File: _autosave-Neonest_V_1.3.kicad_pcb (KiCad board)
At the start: 2 copper layers, 75 x 88 mm, 99 parts, among them J3 693071010811, J5 Conn_01x02, J6 Conn_01x05, J7 Conn_01x03, Q1 BC817, Q2 BC817, Q3 STB33N65M2, Q4 BC817, Q5 STB33N65M2, Q6 STB33N65M2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

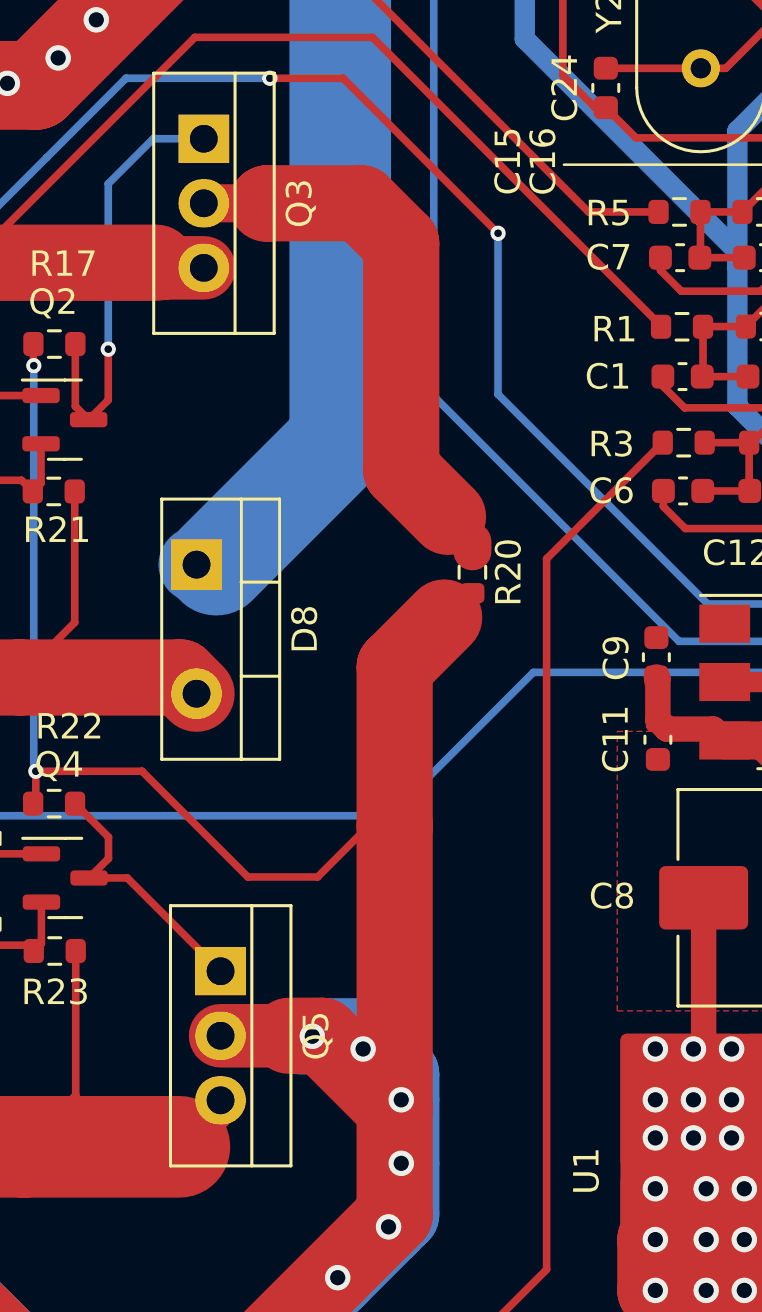
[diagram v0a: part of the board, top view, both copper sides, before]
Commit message: Formatted schematic and Increased power tracks
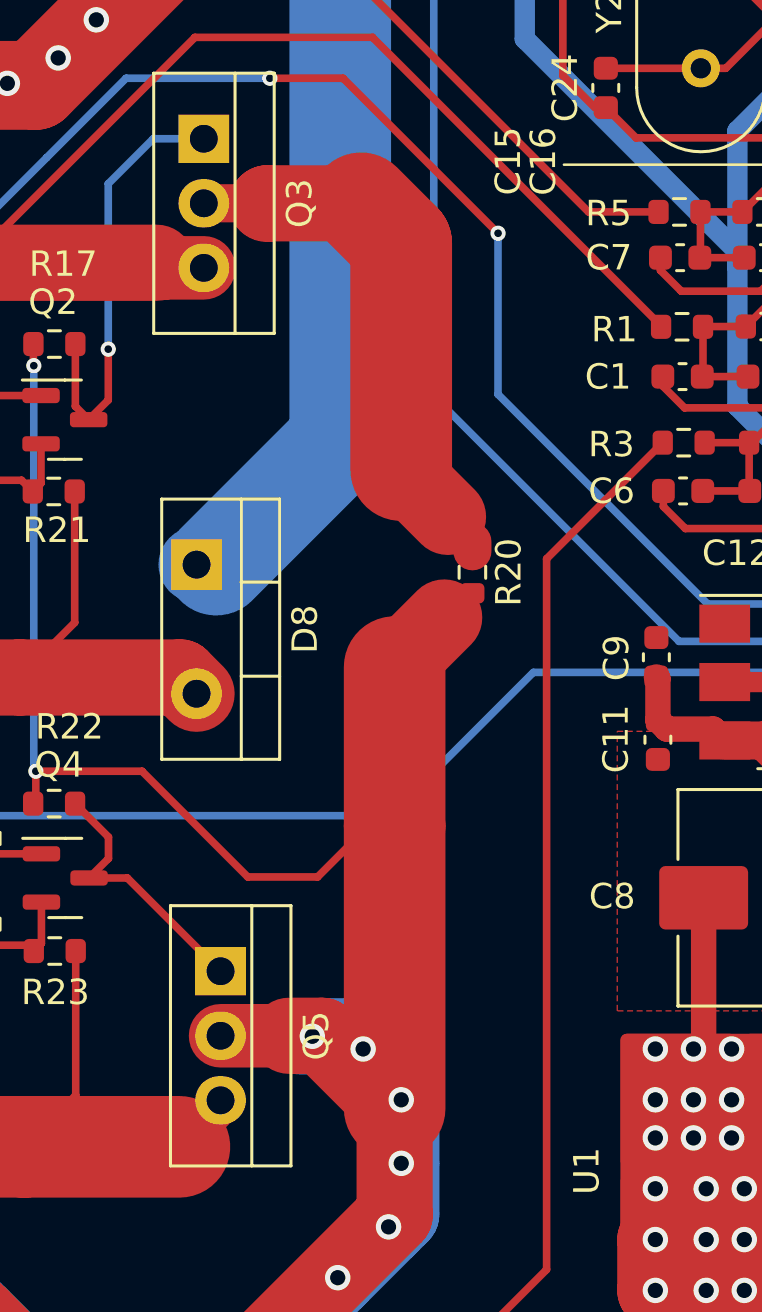
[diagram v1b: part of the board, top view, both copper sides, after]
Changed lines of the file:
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@@
   (segment (start 127.025 86.76) (end 127.025 87.595) (width 0.3) (layer "F.Cu") (net 18))
   (segment (start 134.39 113.98) (end 137.09 113.98) (width 2.5) (layer "F.Cu") (net 18))
-  (segment (start 141.24 116.84) (end 141.24 105.73) (width 3) (layer "F.Cu") (net 18))
+  (segment (start 141.24 116.84) (end 141.24 105.73) (width 4) (layer "F.Cu") (net 18))
   (segment (start 131.3 103.57) (end 135.46 107.73) (width 0.3) (layer "F.Cu") (net 18))
   (segment (start 127.12 103.57) (end 131.3 103.57) (width 0.3) (layer "F.Cu") (net 18))
@@
   (segment (start 134.165 128.29) (end 134.165 128.115) (width 3) (layer "F.Cu") (net 18))
   (segment (start 140.21 105.73) (end 141.24 105.73) (width 0.3) (layer "F.Cu") (net 18))
-  (segment (start 141.24 105.73) (end 141.24 99.47) (width 3) (layer "F.Cu") (net 18))
+  (segment (start 141.24 105.73) (end 141.24 99.47) (width 4) (layer "F.Cu") (net 18))
   (via (at 141.5 119) (size 1) (drill 0.6) (layers "F.Cu" "B.Cu") (net 18))
   (via (at 140 114.5) (size 1) (drill 0.6) (layers "F.Cu" "B.Cu") (net 18))
@@
   (segment (start 129.97 86.96) (end 129.97 80.45) (width 0.3) (layer "B.Cu") (net 41))
   (segment (start 131.74 78.68) (end 133.73 78.68) (width 0.3) (layer "B.Cu") (net 41))
-  (segment (start 139.92 81.22) (end 141.5 82.8) (width 3) (layer "F.Cu") (net 42))
+  (segment (start 139.92 81.22) (end 141.5 82.8) (width 4) (layer "F.Cu") (net 42))
   (segment (start 136.23 81.22) (end 139.92 81.22) (width 3) (layer "F.Cu") (net 42))
   (segment (start 135.32 81.22) (end 135.33 81.23) (width 1.5) (layer "F.Cu") (net 42))
   (segment (start 141.5 91.72) (end 143.34 93.56) (width 3) (layer "F.Cu") (net 42))
   (segment (start 144.3 94.915) (end 144.3 94.535) (width 1.5) (layer "F.Cu") (net 42))
-  (segment (start 141.5 82.8) (end 141.5 91.72) (width 3) (layer "F.Cu") (net 42))
+  (segment (start 141.5 82.8) (end 141.5 91.72) (width 4) (layer "F.Cu") (net 42))
   (segment (start 136.21 81.24) (end 136.23 81.22) (width 3) (layer "F.Cu") (net 42))
   (segment (start 133.73 81.22) (end 135.32 81.22) (width 1.5) (layer "F.Cu") (net 42))
